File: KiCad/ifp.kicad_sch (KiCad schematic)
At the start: 55 parts, among them U1 7815, U10 XPort-01, U2 7915, U3 7805, U4 7805, U5 FT232RL, U6 6N137, U8 LF33, U9 MAX232

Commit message: finishing IFP and starting DCG drawing
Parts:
- added C13: 47µ 6V3, symbol Device:C_Polarized
- added C22: 100n, symbol Device:C
- C1, C23: value 100n ker. RMS -> 100n
- C14: renamed from C22; value 100n ker. RMS -> 100n
- C15: renamed from C18; value 11µ 50V -> 47µ 6V3
- C16: renamed from C17; value 11µ 50V -> 1µ
- C17: renamed from C13; value 47µ 6V3 -> 1µ
- C18: renamed from C15; value 47µ 6V3 -> 1µ
- C19: renamed from C24; value 100n ker. RMS -> 100
- C2: renamed from C5; value 100n ker. RMS -> 100n
- C21: renamed from C16; value 11µ 50V -> 1µ
- C24: renamed from C14; value 100n ker. RMS -> 100n
- C4: renamed from C8; value 100n ker. RMS -> 100n
- R2: renamed from R4; value 2k7 -> 220R
- R3: value 2k2 -> 220R
- R4: renamed from R5; value 2k2 -> 2k7
- renumbered C9 to C10, C4 to C3, C6 to C5, C2 to C6, C3 to C8, C10 to C9, D4 to D1, D1 to D4, JP3 to JP1, JP1 to JP2, JP2 to JP3, R6 to R5, U4 to U3, U3 to U4
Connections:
- net GND: now also C23.1, U5.26 (TEST), C13.2, C22.1; no longer C16.2, C23.2
- net TXD D-Sub: now also U9.7 (T2OUT); no longer U9.14 (T1OUT)
- net VCC: now also C16.1, C13.1, C22.2
- net at U9.10 (T2IN): now also R4.2, U10.4 (Pin_4), U5.5 (RXD), U6.6 (VO)
- net at U9.2 (VS+): now also C16.2; no longer C16.1
- net at RB3.2: now also TR2.6; no longer TR2.5
- net at RB3.4: now also TR2.5; no longer TR2.6
- net at U5.17 (3V3OUT): now also C23.2
- net at TR2.7: now also RB2.4; no longer RB2.2
- net at TR2.8: now also RB2.2; no longer RB2.4
- net at TR1.5: now also RB1.4; no longer RB1.2
- net at TR1.8: now also RB1.2; no longer RB1.4
- net +15V | 1 renamed V++
- net -15V | 1 renamed V--
- net 5V | 2 renamed DVcc
- net 9V | 3 renamed DVgl+
- net GND | 1 renamed AGnd
- net GND | 2 renamed DGnd
- now unconnected: U9.11 (T1IN)
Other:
- moved on the sheet: C16, C23, D3, JP2

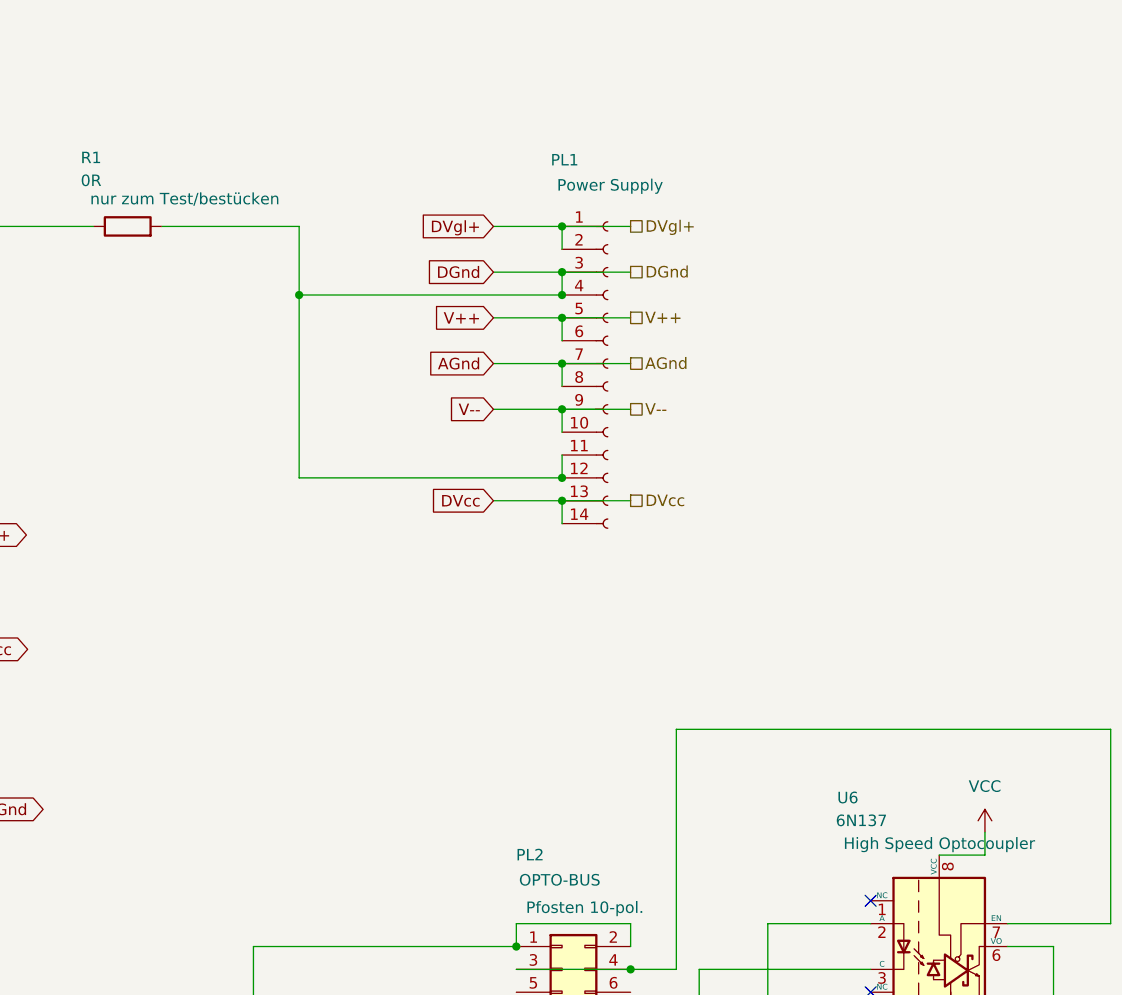
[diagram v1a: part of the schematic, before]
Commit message: drawing ADA/IO schematics
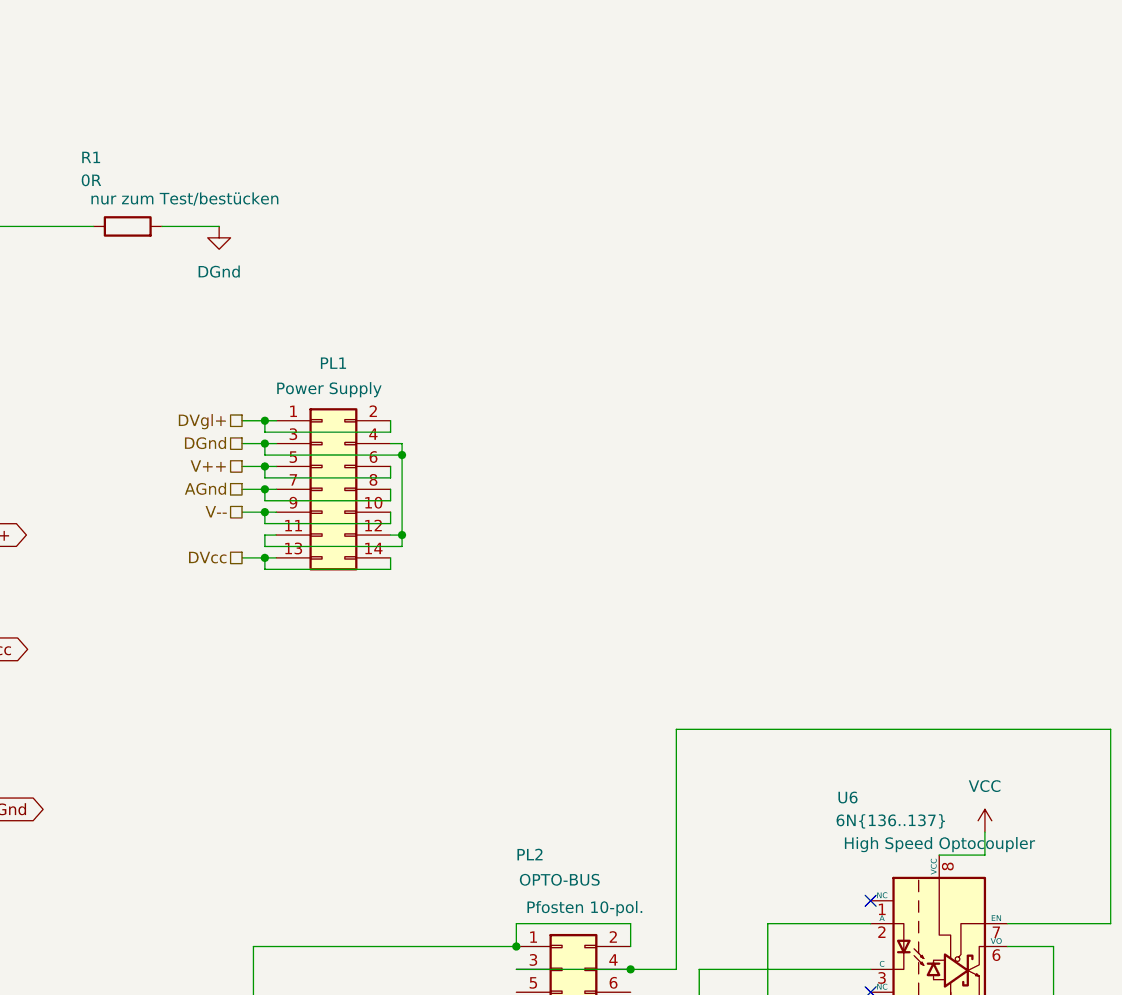
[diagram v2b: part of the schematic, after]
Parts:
- removed PL1: (no value), symbol Connector:Conn_01x14_Socket
- added PL1: Conn_02x07_Odd_Even, symbol Connector_Generic:Conn_02x07_Odd_Even
- U6: value 6N137 -> 6N{136..137}
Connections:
- net AGnd: now also PL1.7 (Pin_7), PL1.8 (Pin_8)
- net DGnd: now also PL1.11 (Pin_11), PL1.12 (Pin_12), PL1.3 (Pin_3), PL1.4 (Pin_4)
- net DVcc: now also PL1.13 (Pin_13), PL1.14 (Pin_14)
- net DVgl+: now also PL1.1 (Pin_1), PL1.2 (Pin_2)
- net V++: now also PL1.5 (Pin_5), PL1.6 (Pin_6)
- net V--: now also PL1.10 (Pin_10), PL1.9 (Pin_9)

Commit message: starting DCG
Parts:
- U10: value XPort-01 -> LF411; footprint (none) -> Package_DIP:DIP-8_W10.16mm
- U5: value FT232RL -> NE5532
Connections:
- net GND: no longer U10.8 (Pin_8), U10.9 (Pin_9), U5.18 (GND), U5.21 (GND), U5.25 (AGND), U5.26 (TEST), U5.7 (GND)
- net VCC: no longer U5.20 (VCC), U5.4 (VCCIO)
- net at R4.2, U6.6 (VO), U9.10 (T2IN): no longer U10.4 (Pin_4), U5.5 (RXD)
- net at U5.1: no longer JP2.1 (A)
- net at PL4.3 (D+): no longer U5.15 (USBD+)
- net at PL4.2 (D-): no longer U5.16 (USBD-)
- net at C23.2: no longer U5.17 (3V3OUT)
- net at R7.2, R8.1: no longer U5.19 (~{RESET})
- net at C15.1, C19.1, U8.1 (VI): no longer U10.7 (Pin_7)
- net at U10.5 (NC): no longer JP3.1 (A)
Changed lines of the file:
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@@
 	)
 	(junction
-		(at 83.82 250.19)
-		(diameter 0)
-		(color 0 0 0 0)
-	)
-	(junction
 		(at 189.23 60.96)
 		(diameter 0)
@@
 	)
 	(junction
-		(at 91.44 250.19)
-		(diameter 0)
-		(color 0 0 0 0)
-	)
-	(junction
 		(at 281.94 123.19)
 		(diameter 0)
@@
 	)
 	(junction
-		(at 27.94 176.53)
-		(diameter 0)
-		(color 0 0 0 0)
-	)
-	(junction
 		(at 241.3 64.77)
 		(diameter 0)
@@
 	)
 	(junction
-		(at 88.9 250.19)
-		(diameter 0)
-		(color 0 0 0 0)
-	)
-	(junction
 		(at 199.39 45.72)
 		(diameter 0)
@@
 	(wire
 		(pts
-			(xy 88.9 250.19) (xy 91.44 250.19)
-		)
-		(stroke
-			(width 0)
-			(type default)
-		)
-	)
-	(wire
-		(pts
 			(xy 50.8 176.53) (xy 66.04 176.53)
 		)
@@
 	(wire
 		(pts
-			(xy 83.82 250.19) (xy 87.63 250.19)
-		)
-		(stroke
-			(width 0)
-			(type default)
-		)
-	)
-	(wire
-		(pts
 			(xy 259.08 198.12) (xy 267.97 198.12)
 		)
@@
 	(wire
 		(pts
-			(xy 83.82 250.19) (xy 68.58 250.19)
+			(xy 68.58 250.19) (xy 87.63 250.19)
 		)
 		(stroke
@@
 	(wire
 		(pts
-			(xy 91.44 250.19) (xy 93.98 250.19)
-		)
-		(stroke
-			(width 0)
-			(type default)
-		)
-	)
-	(wire
-		(pts
 			(xy 114.3 186.69) (xy 114.3 191.77)
 		)
@@
 	(wire
 		(pts
-			(xy 87.63 250.19) (xy 88.9 250.19)
+			(xy 87.63 250.19) (xy 93.98 250.19)
 		)
 		(stroke
@@
 		(dnp no)
 		(property "Reference" "U5"
-			(at 88.646 215.646 0)
+			(at 89.408 223.52 0)
 			(show_name no)
 			(do_not_autoplace no)
@@
 					(size 1.27 1.27)
 				)
+				(justify left)
 			)
 		)
-		(property "Value" "FT232RL"
-			(at 88.646 218.948 0)
+		(property "Value" "NE5532"
+			(at 89.408 226.06 0)
 			(show_name no)
 			(do_not_autoplace no)
@@
 					(size 1.27 1.27)
 				)
+				(justify left)
 			)
 		)
@@
 			)
 		)
-		(property "Datasheet" "https://ftdichip.com/wp-content/uploads/2020/08/DS_FT232R.pdf"
+		(property "Datasheet" "http://www.ti.com/lit/ds/symlink/ne5532.pdf"
 			(at 88.9 224.79 0)
 			(hide yes)
@@
 			)
 		)
-		(property "Description" "USB Controller"
+		(property "Description" "Dual Low-Noise Operational Amplifiers, DIP-8/SOIC-8"
 			(at 88.9 224.79 0)
+			(hide yes)
 			(show_name no)
 			(do_not_autoplace no)
@@
 		(pin "4"
 		)
-		(pin "22"
-		)
-		(pin "13"
-		)
-		(pin "9"
-		)
-		(pin "10"
-		)
-		(pin "12"
-		)
-		(pin "16"
-		)
 		(pin "1"
 		)
@@
 		(pin "3"
 		)
-		(pin "11"
-		)
-		(pin "14"
+		(pin "8"
 		)
 		(pin "6"
 		)
-		(pin "19"
-		)
-		(pin "15"
-		)
-		(pin "20"
-		)
-		(pin "21"
-		)
-		(pin "18"
-		)
-		(pin "17"
-		)
-		(pin "23"
-		)
-		(pin "25"
-		)
-		(pin "26"
-		)
-		(pin "27"
-		)
-		(pin "28"
-		)
 		(instances
 			(project "ctLab"
+				(path "/207e0f0e-27e8-440d-b34e-edbac4dab547/74cd5943-633e-4121-8061-803d69c0160f"
+					(reference "U5")
+					(unit 1)
+				)
 				(path "/207e0f0e-27e8-440d-b34e-edbac4dab547/b26a7a65-419a-400a-bfe0-54512c656443"
 					(reference "U5")
@@
 		(dnp no)
 		(property "Reference" "U10"
-			(at 21.844 149.606 0)
+			(at 30.734 161.798 0)
 			(show_name no)
 			(do_not_autoplace no)
@@
 			)
 		)
-		(property "Value" "XPort-01"
-			(at 24.13 152.4 0)
+		(property "Value" "LF411"
+			(at 31.75 164.4239 0)
 			(show_name no)
 			(do_not_autoplace no)
@@
 			)
 		)
-		(property "Footprint" ""
+		(property "Footprint" "Package_DIP:DIP-8_W10.16mm"
 			(at 22.86 168.91 0)
 			(hide yes)
@@
 			)
 		)
-		(property "Datasheet" ""
+		(property "Datasheet" "https://www.ti.com/lit/gpn/lf411"
 			(at 22.86 168.91 0)
 			(hide yes)
@@
 			)
 		)
-		(property "Description" "Ethernet-Controller"
-			(at 28.956 155.448 0)
+		(property "Description" "FET-Input Operational Amplifier"
+			(at 22.86 168.91 0)
+			(hide yes)
 			(show_name no)
 			(do_not_autoplace no)
@@
 		(pin "4"
 		)
-		(pin "8"
-		)
-		(pin "9"
+		(pin "3"
 		)
 		(pin "6"
@@
 		(instances
 			(project "ctLab"
+				(path "/207e0f0e-27e8-440d-b34e-edbac4dab547/74cd5943-633e-4121-8061-803d69c0160f"
+					(reference "U10")
+					(unit 1)
+				)
 				(path "/207e0f0e-27e8-440d-b34e-edbac4dab547/b26a7a65-419a-400a-bfe0-54512c656443"
 					(reference "U10")

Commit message: cont. dcg schematic
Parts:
- U2: value 7915 -> ATmega32-16M; footprint (none) -> Package_DFN_QFN:QFN-44-1EP_7x7mm_P0.5mm_EP5.2x5.2mm
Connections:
- net AGnd: no longer U2.1 (GND)
- net V--: no longer U2.3 (VO)
- net at C10.2, C4.1, RB1.3 (-): no longer U2.2 (VI)
- new net: U2.17 (VCC), U2.38 (VCC), U2.5 (VCC)
- new net: U2.18 (GND), U2.39 (GND), U2.45 (GND), U2.6 (GND)
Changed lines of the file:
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@@
 		(instances
 			(project "ctLab"
-				(path "/207e0f0e-27e8-440d-b34e-edbac4dab547/74cd5943-633e-4121-8061-803d69c0160f"
-					(reference "U5")
-					(unit 1)
-				)
 				(path "/207e0f0e-27e8-440d-b34e-edbac4dab547/b26a7a65-419a-400a-bfe0-54512c656443"
 					(reference "U5")
@@
 		(pin "7"
 		)
+		(pin "8"
+		)
 		(instances
 			(project "ctLab"
@@
 		(dnp no)
 		(property "Reference" "U2"
-			(at 167.894 66.802 0)
+			(at 179.324 110.744 0)
 			(show_name no)
 			(do_not_autoplace no)
@@
 					(size 1.27 1.27)
 				)
+				(justify left)
 			)
 		)
-		(property "Value" "7915"
-			(at 168.402 69.596 0)
+		(property "Value" "ATmega32-16M"
+			(at 179.324 112.776 0)
 			(show_name no)
 			(do_not_autoplace no)
@@
 					(size 1.27 1.27)
 				)
+				(justify left)
 			)
 		)
-		(property "Footprint" ""
+		(property "Footprint" "Package_DFN_QFN:QFN-44-1EP_7x7mm_P0.5mm_EP5.2x5.2mm"
 			(at 168.91 60.96 0)
 			(hide yes)
@@
 				(font
 					(size 1.27 1.27)
+					(italic yes)
 				)
 			)
 		)
-		(property "Datasheet" "https://www.st.com/resource/en/datasheet/l79.pdf"
+		(property "Datasheet" "http://ww1.microchip.com/downloads/en/DeviceDoc/doc2503.pdf"
 			(at 168.91 60.96 0)
 			(hide yes)
@@
 			)
 		)
-		(property "Description" "-15V Negative voltage regulator"
-			(at 168.656 64.262 0)
+		(property "Description" "16MHz, 32kB Flash, 2kB SRAM, 1kB EEPROM, JTAG, QFN-44"
+			(at 168.91 60.96 0)
+			(hide yes)
 			(show_name no)
 			(do_not_autoplace no)
@@
 		(pin "3"
 		)
+		(pin "17"
+		)
+		(pin "9"
+		)
+		(pin "5"
+		)
+		(pin "7"
+		)
+		(pin "8"
+		)
+		(pin "13"
+		)
+		(pin "14"
+		)
+		(pin "4"
+		)
+		(pin "6"
+		)
+		(pin "12"
+		)
+		(pin "15"
+		)
+		(pin "11"
+		)
+		(pin "18"
+		)
+		(pin "16"
+		)
+		(pin "22"
+		)
+		(pin "23"
+		)
+		(pin "20"
+		)
+		(pin "25"
+		)
+		(pin "10"
+		)
+		(pin "24"
+		)
+		(pin "19"
+		)
+		(pin "21"
+		)
+		(pin "26"
+		)
+		(pin "28"
+		)
+		(pin "27"
+		)
+		(pin "29"
+		)
+		(pin "30"
+		)
+		(pin "31"
+		)
+		(pin "32"
+		)
+		(pin "41"
+		)
+		(pin "38"
+		)
+		(pin "33"
+		)
+		(pin "34"
+		)
+		(pin "40"
+		)
+		(pin "37"
+		)
+		(pin "39"
+		)
+		(pin "36"
+		)
+		(pin "35"
+		)
+		(pin "42"
+		)
+		(pin "43"
+		)
+		(pin "44"
+		)
+		(pin "45"
+		)
 		(instances
 			(project "ctLab"
@@
 			"0c0e42c7-6733-4cdd-8372-9f07dd1f0e7c" "125c0914-30fa-458c-b42c-09fc2910af28"
 			"12838305-ccea-406b-8e78-665344dc4346" "13e784ab-eaa3-4cad-9c5b-32b876ced670"
-			"17abb2d6-27e0-4404-8deb-e5251df35e33" "18823d22-a997-4c84-bdb8-368670da2f60"
 			"25f7298b-ee87-4f27-889e-c7a41e7edf5b" "27afe620-6064-472c-a6c1-53753cc0ffb4"
 			"2c64bc90-8397-40f3-96f7-9ed29fd67946" "30cef4f3-5038-4d06-84f7-84b0fa895db9"
@@
 			"53670da8-4b63-430f-8aeb-9314523b8409" "536832d8-05b8-4f24-b31f-afb639899aea"
 			"569098e7-4c54-40f8-84da-fb3eb065279a" "595e0e39-9c17-41eb-b681-103f6193abec"
-			"5b012770-ad54-43a0-bb30-0d79680adba3" "65a97238-929c-42c2-ad8a-cfb046724b15"
-			"672859a0-46aa-4af1-acdc-863031f07ac8" "69251804-e576-4cf8-99e2-64f8ab1da3d2"
-			"6ce1a0d0-9ba8-4563-ae2b-9e0319c3cf41" "6d27604d-8c47-45f7-ab4d-23dd30945ea4"
-			"709eeaf4-0221-4dc5-b081-b33fd9599ae5" "751bdf5b-319c-4400-9e9f-08e34aefb268"
-			"75f63d2e-972a-423e-a3fd-b3a6efa1e11a" "7d2f51db-78de-4275-bbb1-be40b9644186"
-			"7df529df-19c3-4fb7-9533-e7d43ba75343" "807bc1af-5ba8-46e0-90ba-98895e3da0f9"
-			"819cb86b-7870-4e29-a7f1-f583fa69ef65" "8214da7e-e527-4618-ad1b-277eb10928f6"
-			"86cb3974-30e2-41d4-9daa-5624ed4ef3a9" "8d6dbb8e-7883-4a8a-b413-070a1beafcc2"
-			"94108b59-ab12-4742-b83d-84d9e22ff612" "946b38dc-5669-46fe-889d-c054b5519333"
-			"94d56907-658e-4fd6-8b79-c2c061f5ef34" "96a05d46-1703-45de-a5d7-b117ab6d923e"
+			"5b012770-ad54-43a0-bb30-0d79680adba3" "672859a0-46aa-4af1-acdc-863031f07ac8"
+			"69251804-e576-4cf8-99e2-64f8ab1da3d2" "6ce1a0d0-9ba8-4563-ae2b-9e0319c3cf41"
+			"6d27604d-8c47-45f7-ab4d-23dd30945ea4" "709eeaf4-0221-4dc5-b081-b33fd9599ae5"
+			"751bdf5b-319c-4400-9e9f-08e34aefb268" "75f63d2e-972a-423e-a3fd-b3a6efa1e11a"
+			"7d2f51db-78de-4275-bbb1-be40b9644186" "7df529df-19c3-4fb7-9533-e7d43ba75343"
+			"807bc1af-5ba8-46e0-90ba-98895e3da0f9" "819cb86b-7870-4e29-a7f1-f583fa69ef65"
+			"8214da7e-e527-4618-ad1b-277eb10928f6" "86cb3974-30e2-41d4-9daa-5624ed4ef3a9"
+			"8d6dbb8e-7883-4a8a-b413-070a1beafcc2" "94108b59-ab12-4742-b83d-84d9e22ff612"
+			"946b38dc-5669-46fe-889d-c054b5519333" "96a05d46-1703-45de-a5d7-b117ab6d923e"
 			"98c7760b-6a46-4879-a509-1b365aff2f5a" "991012a4-d2ed-4727-8861-ec050920af6f"
 			"9a58193b-33ad-4894-bb7c-83da7bf44d5e" "9dc4b4d9-01c4-4f40-b683-9c084dd25b53"
-			"9fb6c29f-d630-4160-8daa-90b81796eb18" "a7d75585-74cd-444e-bac8-fbb8c7552f37"
-			"ac893670-8453-4e20-86be-cc590db08a20" "b4c951da-df45-4027-b5e0-72016350ae90"
-			"bcdb9ad2-e608-46ce-b7ce-24f0983f3b13" "c3e4dd71-ea1a-4bfb-af43-a4da5bae3892"
-			"c4c9bd33-cfe2-4282-871b-0057cd7c7217" "c5858ae5-a46d-4355-82aa-e1978e7f536b"
-			"cb9f7e23-6a85-4a85-bfba-476c35f6e543" "ce4adc49-f8a6-4b54-99bb-08ad9b09c64f"
-			"d0b1769f-f840-47d6-b385-56c386204c0c" "d350887e-bfd5-47de-85cc-7490e2593b8b"
+			"9fb6c29f-d630-4160-8daa-90b81796eb18" "ac893670-8453-4e20-86be-cc590db08a20"
+			"b4c951da-df45-4027-b5e0-72016350ae90" "bcdb9ad2-e608-46ce-b7ce-24f0983f3b13"
+			"c3e4dd71-ea1a-4bfb-af43-a4da5bae3892" "c4c9bd33-cfe2-4282-871b-0057cd7c7217"
+			"c5858ae5-a46d-4355-82aa-e1978e7f536b" "cb9f7e23-6a85-4a85-bfba-476c35f6e543"
+			"ce4adc49-f8a6-4b54-99bb-08ad9b09c64f" "d0b1769f-f840-47d6-b385-56c386204c0c"
 			"d837818e-184e-406b-8e26-0814c6f47de0" "dae362ad-317e-4723-9d19-c6fe2ad31a36"
 			"dbb5dd7e-8812-45a3-b4aa-bdfeb18e844d" "dc8cc0fe-9f0f-4149-98de-401c5f060132"

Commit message: Prefix KiCad component references
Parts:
- IFP.U6: renamed from U6; value 6N{136..137} -> LF411; footprint (none) -> Package_DIP:DIP-8_W10.16mm
- renumbered C1 to IFP.C1, C10 to IFP.C10, C11 to IFP.C11, C12 to IFP.C12, C13 to IFP.C13, C14 to IFP.C14, C15 to IFP.C15, C16 to IFP.C16, C17 to IFP.C17, C18 to IFP.C18, C19 to IFP.C19, C2 to IFP.C2, C21 to IFP.C21, C22 to IFP.C22, C23 to IFP.C23, C24 to IFP.C24, C3 to IFP.C3, C4 to IFP.C4, C5 to IFP.C5, C6 to IFP.C6, C7 to IFP.C7, C8 to IFP.C8, C9 to IFP.C9, D1 to IFP.D1, D2 to IFP.D2, D3 to IFP.D3, D4 to IFP.D4, JP1 to IFP.JP1, JP2 to IFP.JP2, JP3 to IFP.JP3, L1 to IFP.L1, PL1 to IFP.PL1, PL2 to IFP.PL2, PL3 to IFP.PL3, PL4 to IFP.PL4, R1 to IFP.R1, R2 to IFP.R2, R3 to IFP.R3, R4 to IFP.R4, R5 to IFP.R5, R7 to IFP.R7, R8 to IFP.R8, RB1 to IFP.RB1, RB2 to IFP.RB2, RB3 to IFP.RB3, RS1 to IFP.RS1, TR1 to IFP.TR1, TR2 to IFP.TR2, U1 to IFP.U1, U10 to IFP.U10, U2 to IFP.U2, U3 to IFP.U3, U4 to IFP.U4, U5 to IFP.U5, U8 to IFP.U8, U9 to IFP.U9
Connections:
- net GND: no longer IFP.U6.5 (GND)
- net VCC: no longer IFP.U6.8 (VCC)
- net at IFP.R4.2, IFP.U9.10 (T2IN): no longer IFP.U6.6 (VO)
- net at IFP.U6.2 (In-): no longer IFP.R2.1
- net at IFP.PL2.7 (Pin_7), IFP.PL2.8 (Pin_8): no longer IFP.U6.3 (C)
- net at IFP.PL2.3 (Pin_3), IFP.PL2.4 (Pin_4): no longer IFP.U6.7 (EN)
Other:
- moved on the sheet: IFP.U10

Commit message: finishing dcg schematic and repairing IFP schematic
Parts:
- removed IFP.U10: LF411, Package_DIP:DIP-8_W10.16mm, symbol Connector:Conn_01x09_Pin
- removed IFP.U2: ATmega32-16M, Package_DFN_QFN:QFN-44-1EP_7x7mm_P0.5mm_EP5.2x5.2mm, symbol Regulator_Linear:L7915
- removed IFP.U5: NE5532, symbol Interface_USB:FT232RL
- added U1: FT232RL, Package_SO:SSOP-28_5.3x10.2mm_P0.65mm, symbol Interface_USB:FT232RL
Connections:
- net GND: now also IFP.U6.4 (VCC-), U1.18 (GND), U1.21 (GND), U1.25 (AGND), U1.26 (TEST), U1.7 (GND)
- net VCC: now also U1.20 (VCC), U1.4 (VCCIO)
- net IFP.PL3:1: now reaches IFP.PL3.1 (Pin_1), IFP.TR1.1, IFP.TR2.1
- net IFP.PL3:2: now reaches IFP.PL3.2 (Pin_2), IFP.TR1.4, IFP.TR2.4
- net IFP.FT232:RXD: now reaches IFP.R4.2, IFP.U9.10 (T2IN)
- net IFP.FT232:RXD: now also U1.5 (RXD)
- net IFP.MAX232.RXD: now reaches IFP.JP1.1 (A), IFP.U9.12 (R1OUT)
- net at IFP.U6.1 (B1): now also IFP.PL2.7 (Pin_7), IFP.PL2.8 (Pin_8)
- net at IFP.U6.2 (In-): now also IFP.R2.1
- net at IFP.PL4.2 (D-): now also U1.16 (USBD-)
- net at IFP.PL4.3 (D+): now also U1.15 (USBD+)
- net IFP.ETH:TXD: now reaches IFP.JP3.1 (A)
- net at IFP.R7.2, IFP.R8.1: now also U1.19 (~{RESET})
- net at IFP.C23.2: now also U1.17 (3V3OUT)
- net IFP.FT232:TXD: now reaches IFP.JP2.1 (A)
- net IFP.FT232:TXD: now also U1.1 (TXD)
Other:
- moved on the sheet: IFP.C13, IFP.C16, IFP.C17, IFP.C18, IFP.C21, IFP.C22, IFP.C23, IFP.C24, IFP.D1, IFP.D2, IFP.D3, IFP.D4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
